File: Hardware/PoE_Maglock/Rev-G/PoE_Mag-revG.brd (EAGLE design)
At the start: 72.8 x 55.2 mm, 90 parts, among them IC2 ATMEGA32U4-MU, J11 1X2-3.5MM, J14 1X2-3.5MM, J15 1X2-3.5MM, J16 1X2-3.5MM, J17 1X2-3.5MM, J2 1X2-3.5MM, J3 1X2-3.5MM, J4 1X2-3.5MM, J5 1X2-3.5MM, J6 10103594-0001LF, Q1 35A/25V/8.5mΩ, Q3 35A/25V/8.5mΩ, Q5 35A/25V/8.5mΩ, Q6 35A/25V/8.5mΩ, SW1 SPST_TACT-KMR2, U4 W5500, X2 J1011FHY931147C, Y4 8MHz

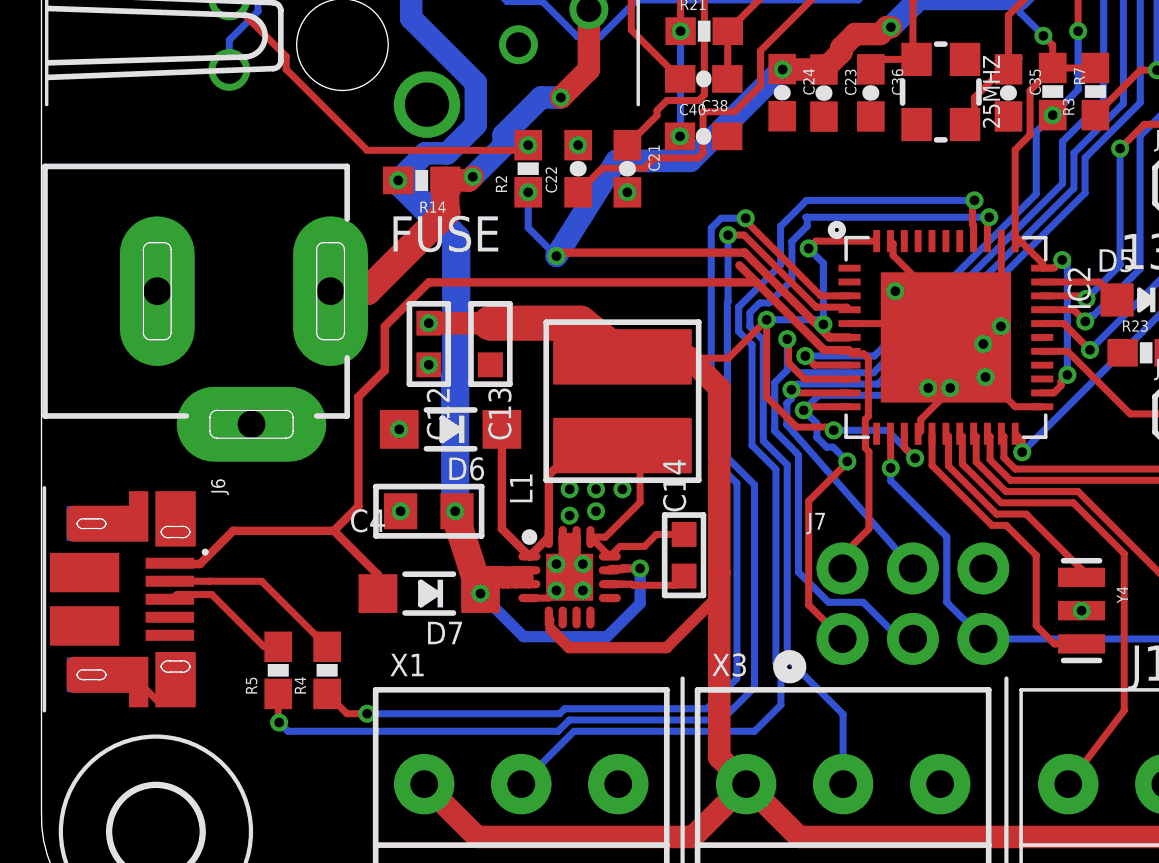
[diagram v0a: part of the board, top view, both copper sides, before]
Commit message: HEEP-1046 dylan approved, init bom csv
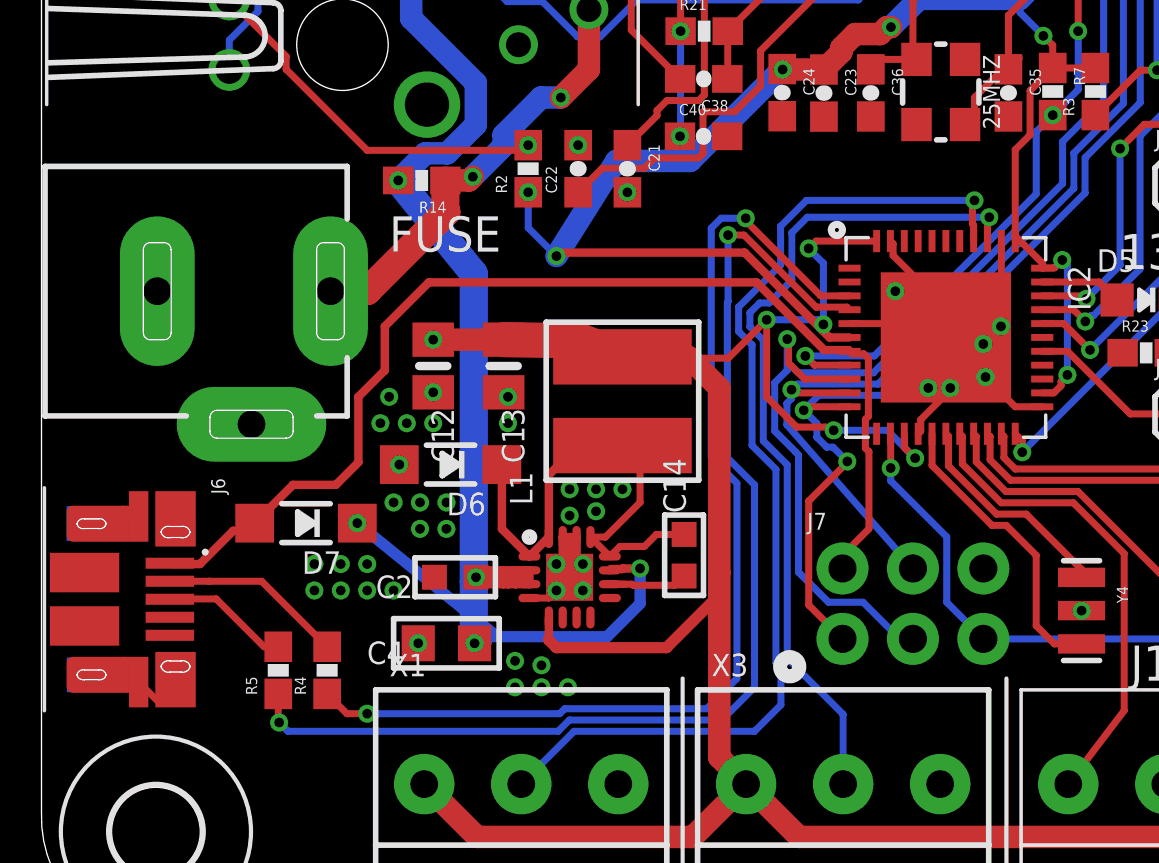
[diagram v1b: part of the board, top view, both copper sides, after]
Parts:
- added C2: .1uF 10V, microbuilder:0603-MINI
- C1: value 100uF 25V -> 100uF 35V
- C12, C13: device microbuilder:0603-MINI -> microbuilder:0805-NO
- moved D7 5.12 mm to (14.0, 14.5)
- moved C4 4.80 mm to (19.1, 10.2)
- moved D6 1.27 mm to (19.2, 16.6)
- moved C13 0.93 mm to (21.1, 20.2)
- moved C12 0.81 mm to (18.6, 20.2)
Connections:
- net GND: now also C2.2
- net VBAT: now also C2.1
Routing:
- net VBAT: track 62.6 -> 67.6 mm, vias 41 -> 42
- net VBUS: track 45.6 -> 40.9 mm
- net N$16: track 20.7 -> 19.4 mm
- net +3V3: track 206.4 -> 205.9 mm
- net GND: vias 103 -> 126
